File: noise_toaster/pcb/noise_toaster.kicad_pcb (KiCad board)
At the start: 2 copper layers, 128 x 129 mm, 133 parts, among them J1 Thonk, J2 Conn_01x02, J3 Thonk, J4 Thonk, Q1 MMBT3904, Q10 MMBT5457, Q2 MMBT3904, Q3 MMBT5457, Q4 MMBT3904, Q5 MMBT3904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

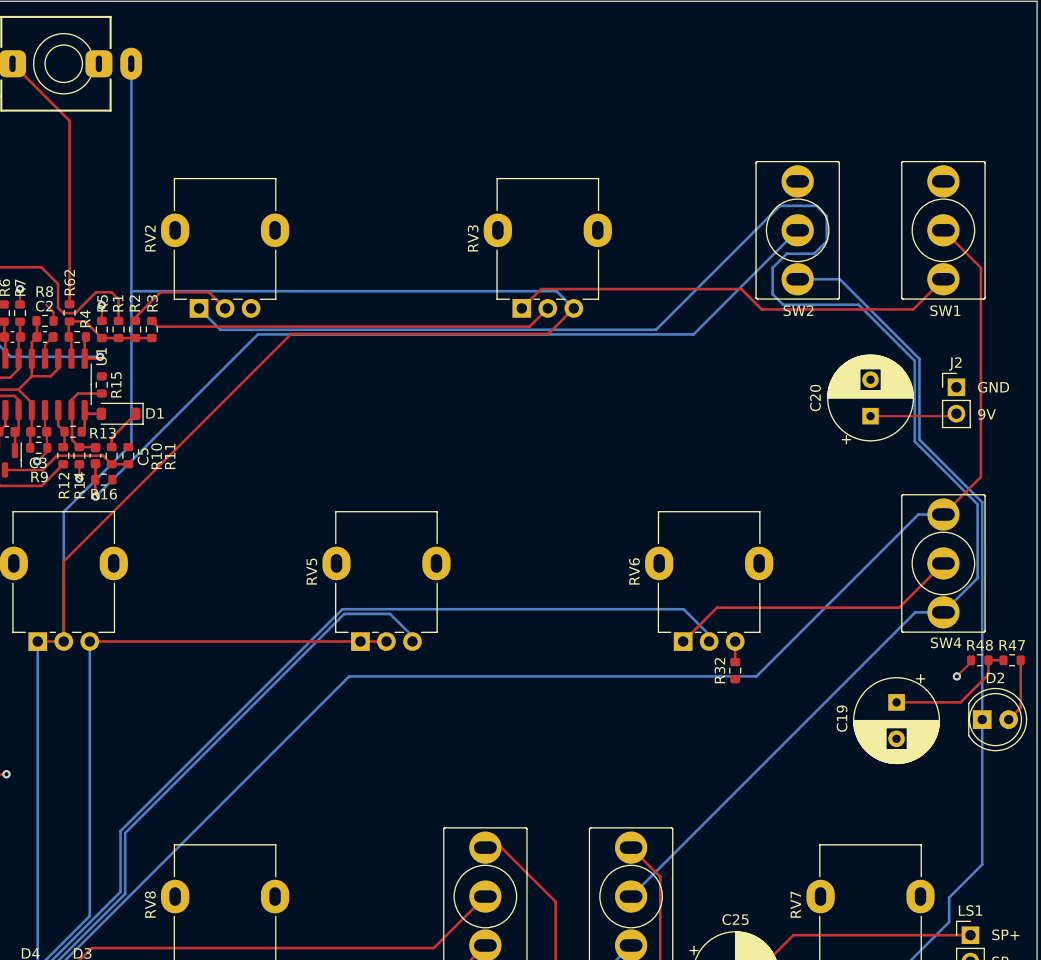
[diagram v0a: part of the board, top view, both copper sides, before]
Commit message: Fixed potentiometer polarities
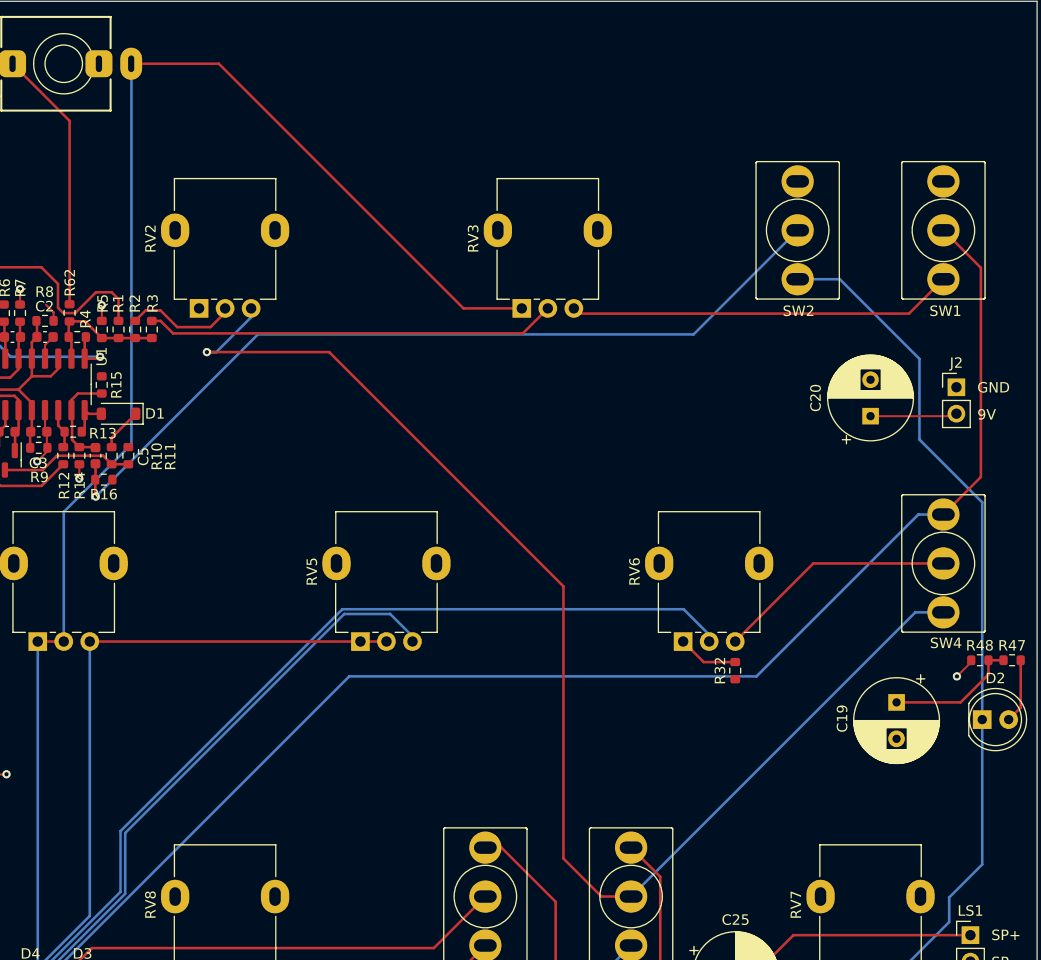
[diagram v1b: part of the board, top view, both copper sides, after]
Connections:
- RV1 pad 1: BP -> BN
- RV1 pad 3: BN -> BP
- RV2 pad 1: LFO -> BN
- RV2 pad 3: BN -> LFO
- RV3 pad 1: Net-(SW1-A) -> GND
- RV3 pad 3: GND -> Net-(SW1-A)
- RV6 pad 1: Net-(SW4-B) -> Net-(R32-Pad2)
- RV6 pad 3: Net-(R32-Pad2) -> Net-(SW4-B)
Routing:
- net GND: track 396.0 -> 333.3 mm
- net LFO: track 163.3 -> 125.5 mm, vias 0 -> 1
- net Net-(SW1-A): track 43.3 -> 37.1 mm
- net Net-(SW4-B): track 28.1 -> 23.1 mm
- net Net-(R32-Pad2): track 1.98 -> 5.82 mm
- net Net-(R3-Pad1): track 39.0 -> 39.5 mm
